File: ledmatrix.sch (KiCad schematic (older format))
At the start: 64 parts, among them U58 sled1735

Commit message: iso/ansi start layout
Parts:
- rgb-ISOh2, rgb-a2, rgb-a3, rgb-b2, rgb-b3, rgb-c1, rgb-c2, rgb-d1, rgb-e1, rgb-f1, rgb-f2, rgb-g1, rgb-g2, rgb-h1, rgb-h2, rgb-i1, rgb-i2, rgb-j1, rgb-j2, rgb-k1, rgb-k2, rgb-l1, rgb-l2, rgb-m1, rgb-m2, rgb-n1, rgb-n2, rgb-o1, rgb-o2, rgb-p1, rgb-p2: footprint raise_fp:3528-4p -> raise_fp:3528-4p-rev

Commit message: switch and led renumbered
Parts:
- rgb10: renamed from rgb-l1; MOQ (none) -> Value; leadtime (none) -> Value; supplier PN (none) -> Value
- rgb11: renamed from rgb-m1; MOQ (none) -> Value; leadtime (none) -> Value; supplier PN (none) -> Value
- rgb12: renamed from rgb-n1; MOQ (none) -> Value; leadtime (none) -> Value; supplier PN (none) -> Value
- rgb13: renamed from rgb-o1; MOQ (none) -> Value; leadtime (none) -> Value; supplier PN (none) -> Value
- rgb14: renamed from rgb-p1; MOQ (none) -> Value; leadtime (none) -> Value; supplier PN (none) -> Value
- rgb15: renamed from rgb-a2; MOQ (none) -> Value; leadtime (none) -> Value; supplier PN (none) -> Value
- rgb16: renamed from rgb-b2; MOQ (none) -> Value; leadtime (none) -> Value; supplier PN (none) -> Value
- rgb17: renamed from rgb-c2; MOQ (none) -> Value; leadtime (none) -> Value; supplier PN (none) -> Value
- rgb18: renamed from rgb-f2; MOQ (none) -> Value; leadtime (none) -> Value; supplier PN (none) -> Value
- rgb19: renamed from rgb-g2; MOQ (none) -> Value; leadtime (none) -> Value; supplier PN (none) -> Value
- rgb2: renamed from rgb-d1; MOQ (none) -> Value; leadtime (none) -> Value; supplier PN (none) -> Value
- rgb20: renamed from rgb-h2; MOQ (none) -> Value; leadtime (none) -> Value; supplier PN (none) -> Value
- rgb21: renamed from rgb-i2; MOQ (none) -> Value; leadtime (none) -> Value; supplier PN (none) -> Value
- rgb22: renamed from rgb-j2; MOQ (none) -> Value; leadtime (none) -> Value; supplier PN (none) -> Value
- rgb23: renamed from rgb-k2; MOQ (none) -> Value; leadtime (none) -> Value; supplier PN (none) -> Value
- rgb24: renamed from rgb-l2; MOQ (none) -> Value; leadtime (none) -> Value; supplier PN (none) -> Value
- rgb25: renamed from rgb-m2; MOQ (none) -> Value; leadtime (none) -> Value; supplier PN (none) -> Value
- rgb26: renamed from rgb-n2; MOQ (none) -> Value; leadtime (none) -> Value; supplier PN (none) -> Value
- rgb27: renamed from rgb-o2; MOQ (none) -> Value; leadtime (none) -> Value; supplier PN (none) -> Value
- rgb28: renamed from rgb-p2; MOQ (none) -> Value; leadtime (none) -> Value; supplier PN (none) -> Value
- rgb29: renamed from rgb-a3; MOQ (none) -> Value; leadtime (none) -> Value; supplier PN (none) -> Value
- rgb3: renamed from rgb-e1; MOQ (none) -> Value; leadtime (none) -> Value; supplier PN (none) -> Value
- rgb30: renamed from rgb-b3; MOQ (none) -> Value; leadtime (none) -> Value; supplier PN (none) -> Value
- rgb31: renamed from rgb-c3; footprint raise_fp:3528-4p -> raise_fp:3528-4p-rev; MOQ (none) -> Value; leadtime (none) -> Value; supplier PN (none) -> Value
- rgb32: renamed from rgb-d3; MOQ (none) -> Value; leadtime (none) -> Value; supplier PN (none) -> Value
- rgb33: renamed from rgb-e3; MOQ (none) -> Value; leadtime (none) -> Value; supplier PN (none) -> Value
- rgb34: renamed from rgb-f3; MOQ (none) -> Value; leadtime (none) -> Value; supplier PN (none) -> Value
- rgb35: renamed from rgb-i3; MOQ (none) -> Value; leadtime (none) -> Value; supplier PN (none) -> Value
- rgb36: renamed from rgb-j3; MOQ (none) -> Value; leadtime (none) -> Value; supplier PN (none) -> Value
- rgb37: renamed from rgb-k3; MOQ (none) -> Value; leadtime (none) -> Value; supplier PN (none) -> Value
- rgb38: renamed from rgb-l3; MOQ (none) -> Value; leadtime (none) -> Value; supplier PN (none) -> Value
- rgb39: renamed from rgb-m3; MOQ (none) -> Value; leadtime (none) -> Value; supplier PN (none) -> Value
- rgb4: renamed from rgb-f1; MOQ (none) -> Value; leadtime (none) -> Value; supplier PN (none) -> Value
- rgb40: renamed from rgb-n3; MOQ (none) -> Value; leadtime (none) -> Value; supplier PN (none) -> Value
- rgb41: renamed from rgb-o3; MOQ (none) -> Value; leadtime (none) -> Value; supplier PN (none) -> Value
- rgb42: renamed from rgb-p3; MOQ (none) -> Value; leadtime (none) -> Value; supplier PN (none) -> Value
- rgb43: renamed from rgb-a4; MOQ (none) -> Value; leadtime (none) -> Value; supplier PN (none) -> Value
- rgb44: renamed from rgb-b4; MOQ (none) -> Value; leadtime (none) -> Value; supplier PN (none) -> Value
- rgb45: renamed from rgb-c4; MOQ (none) -> Value; leadtime (none) -> Value; supplier PN (none) -> Value
- rgb46: renamed from rgb-d4; MOQ (none) -> Value; leadtime (none) -> Value; supplier PN (none) -> Value
- rgb47: renamed from rgb-e4; MOQ (none) -> Value; leadtime (none) -> Value; supplier PN (none) -> Value
- rgb48: renamed from rgb-f4; MOQ (none) -> Value; leadtime (none) -> Value; supplier PN (none) -> Value
- rgb49: renamed from rgb-g4; MOQ (none) -> Value; leadtime (none) -> Value; supplier PN (none) -> Value
- rgb5: renamed from rgb-g1; MOQ (none) -> Value; leadtime (none) -> Value; supplier PN (none) -> Value
- rgb50: renamed from rgb-h4; MOQ (none) -> Value; leadtime (none) -> Value; supplier PN (none) -> Value
- rgb51: renamed from rgb-i4; MOQ (none) -> Value; leadtime (none) -> Value; supplier PN (none) -> Value
- rgb52: renamed from rgb-l4; MOQ (none) -> Value; leadtime (none) -> Value; supplier PN (none) -> Value
- rgb53: renamed from rgb-m4; MOQ (none) -> Value; leadtime (none) -> Value; supplier PN (none) -> Value
- rgb54: renamed from rgb-n4; MOQ (none) -> Value; leadtime (none) -> Value; supplier PN (none) -> Value
- rgb55: renamed from rgb-o4; MOQ (none) -> Value; leadtime (none) -> Value; supplier PN (none) -> Value
- rgb56: renamed from rgb-p4; MOQ (none) -> Value; leadtime (none) -> Value; supplier PN (none) -> Value
- rgb57: renamed from rgb-a5; MOQ (none) -> Value; leadtime (none) -> Value; supplier PN (none) -> Value
- rgb58: renamed from rgb-b5; MOQ (none) -> Value; leadtime (none) -> Value; supplier PN (none) -> Value
- rgb59: renamed from rgb-c5; MOQ (none) -> Value; leadtime (none) -> Value; supplier PN (none) -> Value
- rgb6: renamed from rgb-h1; MOQ (none) -> Value; leadtime (none) -> Value; supplier PN (none) -> Value
- rgb7: renamed from rgb-i1; MOQ (none) -> Value; leadtime (none) -> Value; supplier PN (none) -> Value
- rgb8: renamed from rgb-j1; MOQ (none) -> Value; leadtime (none) -> Value; supplier PN (none) -> Value
- rgb9: renamed from rgb-k1; MOQ (none) -> Value; leadtime (none) -> Value; supplier PN (none) -> Value
- renumbered C3 to C6, rgb-ISOh2 to rgb-ISO-20, rgb-c1 to rgb1, rgb-d5 to rgb60, rgb-e5 to rgb61

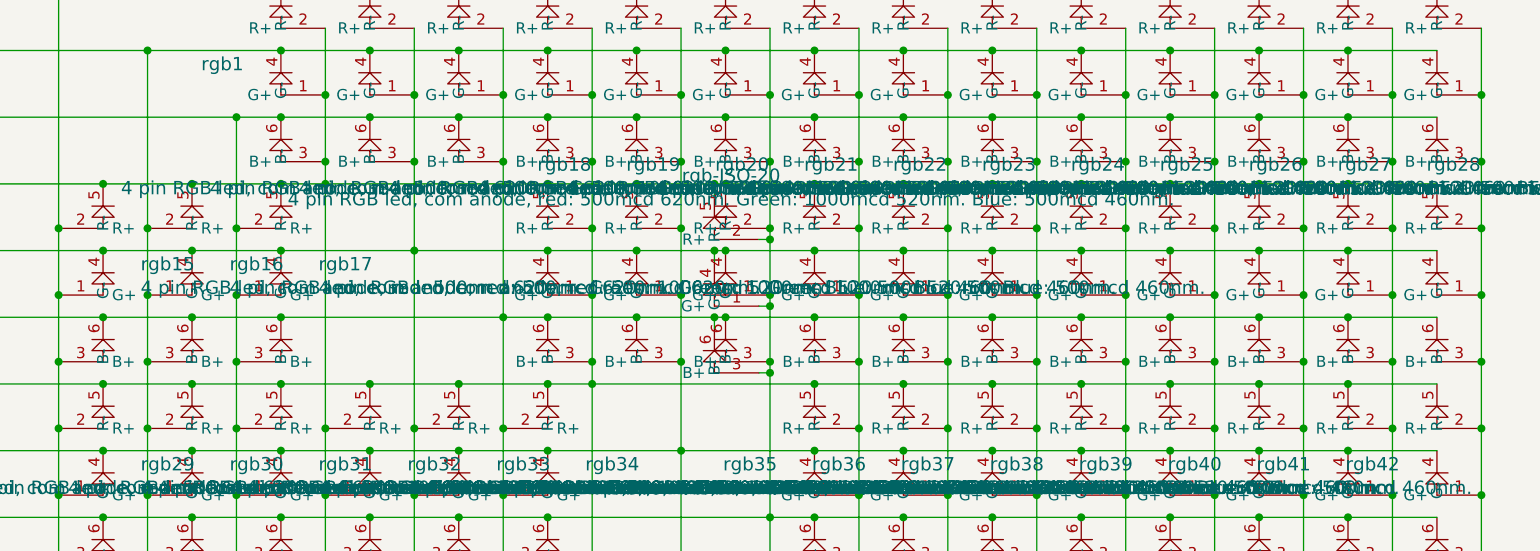
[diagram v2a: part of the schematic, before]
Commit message: led iso/ansi numbering
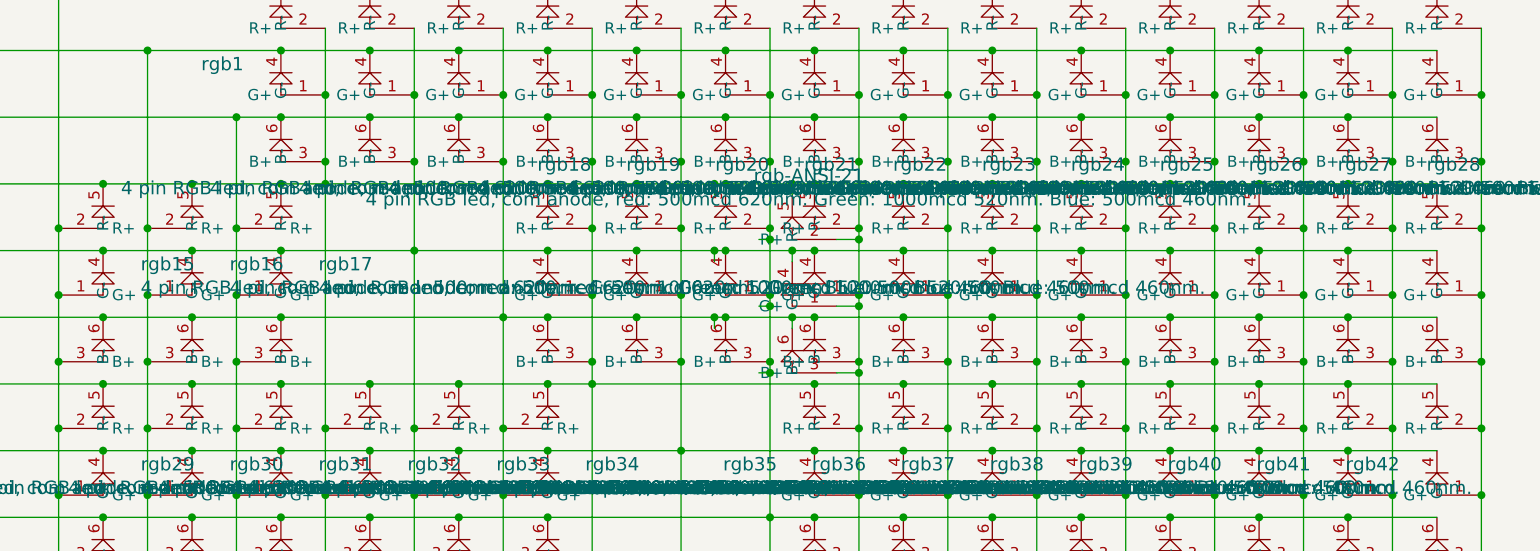
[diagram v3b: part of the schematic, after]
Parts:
- renumbered rgb-ISO-20 to rgb-ANSI-21
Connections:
- wire segments 48 -> 54
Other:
- moved on the sheet: rgb-ANSI-21
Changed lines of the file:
@@
 EESchema Schematic File Version 3
 LIBS:raise-left-rescue
-LIBS:power
-LIBS:74xx
 LIBS:raise-left-cache
 EELAYER 26 0
@@
 $EndComp
 $Comp
-L rgbled rgb-ISO-20
+L rgbled rgb-ANSI-21
 U 1 1 5AE32BA1
-P 4300 2450
-F 0 "rgb-ISO-20" H 4375 3037 60  0000 C CNN
-F 1 "4 pin RGB led, com anode, red: 500mcd 620nm. Green: 1000mcd 520nm. Blue: 500mcd 460nm." H 4375 2931 60  0000 C CNN
-F 2 "raise_fp:3528-4p-rev" H 4300 2450 60  0001 C CNN
-F 3 "" H 4300 2450 60  0001 C CNN
-F 4 "any/open" H -50 50  60  0001 C CNN "supplier"
-F 5 "Value" H 4300 2450 60  0001 C CNN "supplier PN"
-F 6 "Value" H 4300 2450 60  0001 C CNN "MOQ"
-F 7 "Value" H 4300 2450 60  0001 C CNN "leadtime"
-	1    4300 2450
+P 4650 2450
+F 0 "rgb-ANSI-21" H 4725 3037 60  0000 C CNN
+F 1 "4 pin RGB led, com anode, red: 500mcd 620nm. Green: 1000mcd 520nm. Blue: 500mcd 460nm." H 4725 2931 60  0000 C CNN
+F 2 "raise_fp:3528-4p-rev" H 4650 2450 60  0001 C CNN
+F 3 "" H 4650 2450 60  0001 C CNN
+F 4 "any/open" H 300 50  60  0001 C CNN "supplier"
+F 5 "Value" H 4650 2450 60  0001 C CNN "supplier PN"
+F 6 "Value" H 4650 2450 60  0001 C CNN "MOQ"
+F 7 "Value" H 4650 2450 60  0001 C CNN "leadtime"
+	1    4650 2450
 	1    0    0    -1
 $EndComp
@@
 	4500 2750 4550 2750
 Connection ~ 4550 2750
+Wire Wire Line
+	4850 2150 4950 2150
+Connection ~ 4950 2150
+Wire Wire Line
+	4850 2450 4950 2450
+Connection ~ 4950 2450
+Wire Wire Line
+	4850 2750 4950 2750
+Connection ~ 4950 2750
+Wire Wire Line
+	4650 2550 4650 2500
+Connection ~ 4650 2500
+Wire Wire Line
+	4650 2250 4650 2200
+Connection ~ 4650 2200
+Wire Wire Line
+	4650 1950 4650 1900
+Connection ~ 4650 1900
 $EndSCHEMATC

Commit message: post align
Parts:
- renumbered rgb-ANSI-21 to rgb_ANSI_21
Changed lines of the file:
@@
 $EndComp
 $Comp
-L rgbled rgb-ANSI-21
+L rgbled rgb_ANSI_21
 U 1 1 5AE32BA1
 P 4650 2450
-F 0 "rgb-ANSI-21" H 4725 3037 60  0000 C CNN
+F 0 "rgb_ANSI_21" H 4725 3037 60  0000 C CNN
 F 1 "4 pin RGB led, com anode, red: 500mcd 620nm. Green: 1000mcd 520nm. Blue: 500mcd 460nm." H 4725 2931 60  0000 C CNN
 F 2 "raise_fp:3528-4p-rev" H 4650 2450 60  0001 C CNN

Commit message: new alignment
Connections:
- net labels added: cb7, cb8
- net labels removed: cb1, cb2
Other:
- note added: "for leds 62, 63 (o5, p5)\n\n"
- note removed: "for leds j5 k5"
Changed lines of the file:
@@
 Text Notes 2200 300  0    197  ~ 0
 common anode type 3 matrix
-Text Label 4100 6600 2    60   ~ 0
-CB1
-Text Label 4100 6700 2    60   ~ 0
-CB2
-Text Label 4100 6100 2    60   ~ 0
+Text Label 6050 6600 2    60   ~ 0
+CB7
+Text Label 6050 6700 2    60   ~ 0
+CB8
+Text Label 6050 6100 2    60   ~ 0
 CB4
-Text Label 4100 6200 2    60   ~ 0
+Text Label 6050 6200 2    60   ~ 0
 CB5
-Text Label 4100 6300 2    60   ~ 0
+Text Label 6050 6300 2    60   ~ 0
 CB6
 Wire Wire Line
-	4100 6100 3750 6100
+	6050 6100 5700 6100
 Wire Wire Line
-	3750 6200 4100 6200
+	5700 6200 6050 6200
 Wire Wire Line
-	4100 6300 3750 6300
+	6050 6300 5700 6300
 Wire Wire Line
-	4100 6600 3750 6600
+	6050 6600 5700 6600
 Wire Wire Line
-	3750 6700 4100 6700
+	5700 6700 6050 6700
 Text Notes 7650 850  2    236  ~ 0
 A B C D E F G H I J K L M N O P
@@
 Text Notes 750  5500 2    197  ~ 0
 1\n2\n3\n4\n5\n6\n7\n8\n9\n10\n11\n12\n13\n14\n15
-Text Notes 3550 5950 0    60   ~ 0
-for leds  j5 k5
-Text GLabel 3750 6100 0    60   Input ~ 0
+Text Notes 6400 6500 0    60   ~ 0
+for leds  62, 63 (o5, p5)\n\n
+Text GLabel 5700 6100 0    60   Input ~ 0
 cb4
-Text GLabel 3750 6200 0    60   Input ~ 0
+Text GLabel 5700 6200 0    60   Input ~ 0
 cb5
-Text GLabel 3750 6300 0    60   Input ~ 0
+Text GLabel 5700 6300 0    60   Input ~ 0
 cb6
-Text GLabel 3750 6600 0    60   Input ~ 0
-cb1
-Text GLabel 3750 6700 0    60   Input ~ 0
-cb2
+Text GLabel 5700 6600 0    60   Input ~ 0
+cb7
+Text GLabel 5700 6700 0    60   Input ~ 0
+cb8
 $Comp
 L Earth #PWR031
@@
 $EndComp
 Wire Notes Line
-	5550 4750 5550 6300
+	7500 4750 7500 6300
 Wire Notes Line
-	5550 6300 4400 6300
+	7500 6300 6350 6300
 Wire Notes Line
-	5150 4750 5150 6250
+	7100 4750 7100 6250
 $Comp
 L rgbled rgb1

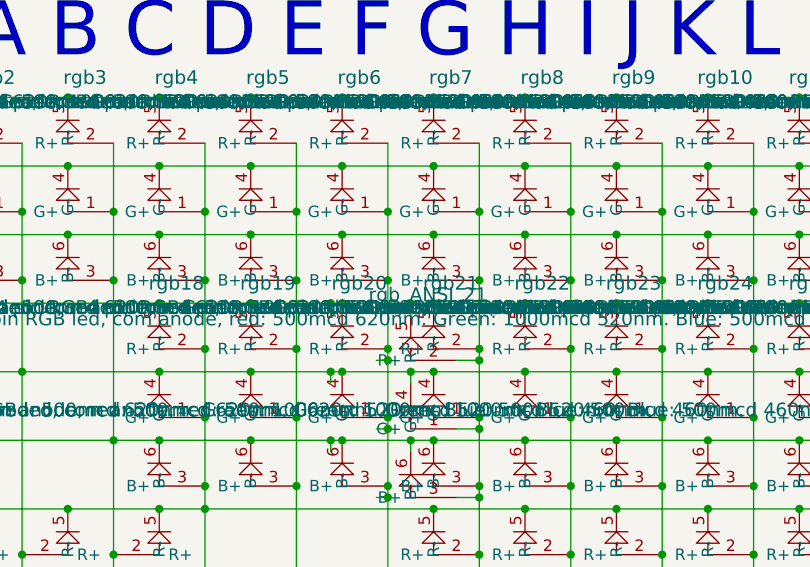
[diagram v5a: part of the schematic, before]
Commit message: iso/ansi component naming
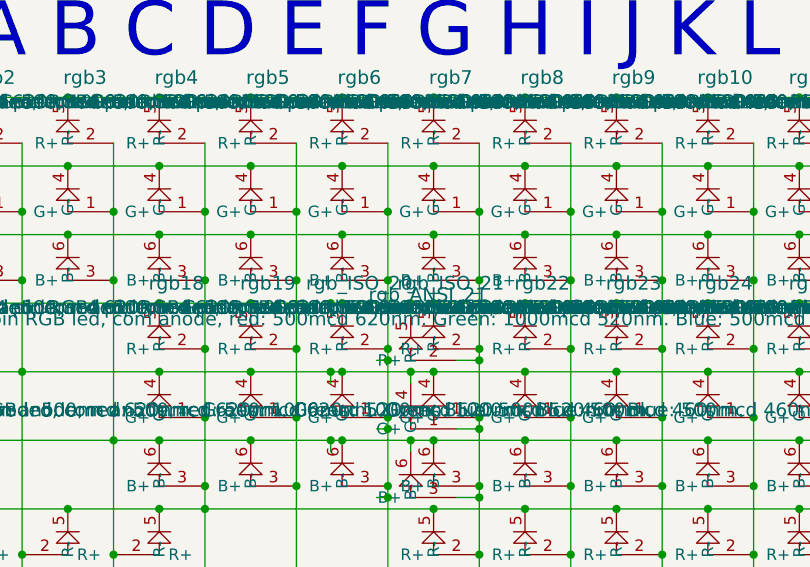
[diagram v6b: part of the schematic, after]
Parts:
- renumbered rgb20 to rgb_ISO_20, rgb21 to rgb_ISO_21
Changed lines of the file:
@@
 $EndComp
 $Comp
-L rgbled rgb20
+L rgbled rgb_ISO_20
 U 1 1 5AD8308C
 P 4350 2400
-F 0 "rgb20" H 4425 2987 60  0000 C CNN
+F 0 "rgb_ISO_20" H 4425 2987 60  0000 C CNN
 F 1 "4 pin RGB led, com anode, red: 500mcd 620nm. Green: 1000mcd 520nm. Blue: 500mcd 460nm." H 4425 2881 60  0000 C CNN
 F 2 "raise_fp:3528-4p-rev" H 4350 2400 60  0001 C CNN
@@
 $EndComp
 $Comp
-L rgbled rgb21
+L rgbled rgb_ISO_21
 U 1 1 59AED4A7
 P 4750 2400
-F 0 "rgb21" H 4825 2987 60  0000 C CNN
+F 0 "rgb_ISO_21" H 4825 2987 60  0000 C CNN
 F 1 "4 pin RGB led, com anode, red: 500mcd 620nm. Green: 1000mcd 520nm. Blue: 500mcd 460nm." H 4825 2881 60  0000 C CNN
 F 2 "raise_fp:3528-4p-rev" H 4750 2400 60  0001 C CNN

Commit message: pre autoroute
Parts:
- removed rgb32, rgb33, rgb34: 4 pin RGB led, com anode, red: 500mcd 620nm. Gree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, raise_fp:3528-4p, symbol rgbled
- added rgb62, rgb63, rgb64: 4 pin RGB led, com anode, red: 500mcd 620nm. Gree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, raise_fp:3528-4p, symbol rgbled
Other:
- note added: "normal mount\nunderglow"
- note added: "reverse mount\nkeys"
- note added: "reverse mount\nlow profile"
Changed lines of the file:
@@
-	-1   0    0    -1
-$EndComp
-$Comp
-L rgbled rgb32
-U 1 1 5AD77B86
-P 2750 3300
-F 0 "rgb32" H 2581 3439 60  0000 R CNN
-F 1 "4 pin RGB led, com anode, red: 500mcd 620nm. Green: 1000mcd 520nm. Blue: 500mcd 460nm." H 2581 3333 60  0000 R CNN
-F 2 "raise_fp:3528-4p" H 2750 3300 60  0001 C CNN
-F 3 "" H 2750 3300 60  0001 C CNN
-F 4 "any/open" H 0   0   60  0001 C CNN "supplier"
-F 5 "Value" H 2750 3300 60  0001 C CNN "supplier PN"
-F 6 "Value" H 2750 3300 60  0001 C CNN "MOQ"
-F 7 "Value" H 2750 3300 60  0001 C CNN "leadtime"
-	1    2750 3300
-	-1   0    0    -1
-$EndComp
-$Comp
-L rgbled rgb33
-U 1 1 5AD77B8D
-P 3150 3300
-F 0 "rgb33" H 2981 3439 60  0000 R CNN
-F 1 "4 pin RGB led, com anode, red: 500mcd 620nm. Green: 1000mcd 520nm. Blue: 500mcd 460nm." H 2981 3333 60  0000 R CNN
-F 2 "raise_fp:3528-4p" H 3150 3300 60  0001 C CNN
-F 3 "" H 3150 3300 60  0001 C CNN
-F 4 "any/open" H 0   0   60  0001 C CNN "supplier"
-F 5 "Value" H 3150 3300 60  0001 C CNN "supplier PN"
-F 6 "Value" H 3150 3300 60  0001 C CNN "MOQ"
-F 7 "Value" H 3150 3300 60  0001 C CNN "leadtime"
-	1    3150 3300
-	-1   0    0    -1
-$EndComp
-$Comp
-L rgbled rgb34
-U 1 1 5AD77B94
-P 3550 3300
-F 0 "rgb34" H 3381 3439 60  0000 R CNN
-F 1 "4 pin RGB led, com anode, red: 500mcd 620nm. Green: 1000mcd 520nm. Blue: 500mcd 460nm." H 3381 3333 60  0000 R CNN
-F 2 "raise_fp:3528-4p" H 3550 3300 60  0001 C CNN
-F 3 "" H 3550 3300 60  0001 C CNN
-F 4 "any/open" H 0   0   60  0001 C CNN "supplier"
-F 5 "Value" H 3550 3300 60  0001 C CNN "supplier PN"
-F 6 "Value" H 3550 3300 60  0001 C CNN "MOQ"
-F 7 "Value" H 3550 3300 60  0001 C CNN "leadtime"
-	1    3550 3300
 	-1   0    0    -1
 $EndComp
@@
 	4650 1950 4650 1900
 Connection ~ 4650 1900
+$Comp
+L rgbled rgb62
+U 1 1 5B34A670
+P 3550 5100
+F 0 "rgb62" H 3381 5239 60  0000 R CNN
+F 1 "4 pin RGB led, com anode, red: 500mcd 620nm. Green: 1000mcd 520nm. Blue: 500mcd 460nm." H 3381 5133 60  0000 R CNN
+F 2 "raise_fp:3528-4p" H 3550 5100 60  0001 C CNN
+F 3 "" H 3550 5100 60  0001 C CNN
+F 4 "any/open" H 800 0   60  0001 C CNN "supplier"
+F 5 "Value" H 3550 5100 60  0001 C CNN "supplier PN"
+F 6 "Value" H 3550 5100 60  0001 C CNN "MOQ"
+F 7 "Value" H 3550 5100 60  0001 C CNN "leadtime"
+	1    3550 5100
+	-1   0    0    -1
+$EndComp
+$Comp
+L rgbled rgb63
+U 1 1 5B34A794
+P 3950 5100
+F 0 "rgb63" H 3781 5239 60  0000 R CNN
+F 1 "4 pin RGB led, com anode, red: 500mcd 620nm. Green: 1000mcd 520nm. Blue: 500mcd 460nm." H 3781 5133 60  0000 R CNN
+F 2 "raise_fp:3528-4p" H 3950 5100 60  0001 C CNN
+F 3 "" H 3950 5100 60  0001 C CNN
+F 4 "any/open" H 1200 0   60  0001 C CNN "supplier"
+F 5 "Value" H 3950 5100 60  0001 C CNN "supplier PN"
+F 6 "Value" H 3950 5100 60  0001 C CNN "MOQ"
+F 7 "Value" H 3950 5100 60  0001 C CNN "leadtime"
+	1    3950 5100
+	-1   0    0    -1
+$EndComp
+$Comp
+L rgbled rgb64
+U 1 1 5B34A8B2
+P 4350 5100
+F 0 "rgb64" H 4181 5239 60  0000 R CNN
+F 1 "4 pin RGB led, com anode, red: 500mcd 620nm. Green: 1000mcd 520nm. Blue: 500mcd 460nm." H 4181 5133 60  0000 R CNN
+F 2 "raise_fp:3528-4p" H 4350 5100 60  0001 C CNN
+F 3 "" H 4350 5100 60  0001 C CNN
+F 4 "any/open" H 1600 0   60  0001 C CNN "supplier"
+F 5 "Value" H 4350 5100 60  0001 C CNN "supplier PN"
+F 6 "Value" H 4350 5100 60  0001 C CNN "MOQ"
+F 7 "Value" H 4350 5100 60  0001 C CNN "leadtime"
+	1    4350 5100
+	-1   0    0    -1
+$EndComp
+Wire Notes Line
+	4700 2900 7500 2900
+Wire Notes Line
+	7500 2900 7500 4550
+Wire Notes Line
+	7500 4550 4450 4550
+Wire Notes Line
+	4450 4550 4450 5350
+Wire Notes Line
+	4450 5350 1450 5350
+Wire Notes Line
+	1450 5350 1450 3800
+Wire Notes Line
+	1450 3800 4650 3800
+Wire Notes Line
+	4650 3800 4650 2900
+Text Notes 5050 3900 0    60   ~ 0
+normal mount\nunderglow
+Text Notes 1400 1300 0    60   ~ 0
+reverse mount\nkeys
+Text Notes 7000 4750 0    60   ~ 0
+reverse mount\nlow profile
 $EndSCHEMATC

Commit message: ansi/iso bom
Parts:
- U58: symbol sled1735-RESCUE-raise-left -> sled1735
- rgb1, rgb10, rgb11, rgb12, rgb13, rgb14, rgb15, rgb16, rgb17, rgb18, rgb19, rgb2, rgb22, rgb23, rgb24, rgb25, rgb26, rgb27, rgb28, rgb29, rgb3, rgb30, rgb31, rgb4, rgb5, rgb6, rgb7, rgb8, rgb9, rgb_ANSI_21, rgb_ISO_20, rgb_ISO_21: value 4 pin RGB led, com anode, red: 500mcd 620nm. Green: 1000mcd 520nm. Blue: 500mcd 460nm. -> reverse 4 pin RGB led, com anode
- rgb35, rgb36, rgb37, rgb38, rgb39, rgb40, rgb41, rgb42, rgb43, rgb44, rgb45, rgb46, rgb47, rgb48, rgb49, rgb50, rgb51, rgb52, rgb53, rgb54, rgb55, rgb56, rgb57, rgb58, rgb59, rgb60, rgb61, rgb62, rgb63, rgb64: value 4 pin RGB led, com anode, red: 500mcd 620nm. Green: 1000mcd 520nm. Blue: 500mcd 460nm. -> 4 pin RGB led, com anode
